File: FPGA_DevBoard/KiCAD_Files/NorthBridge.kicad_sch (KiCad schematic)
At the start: 15 parts, among them J1 4677, J2 DM3D-SF, U1 W25Q128JVSIQ TR, U14 ESP32-WROOM-32UE-N8

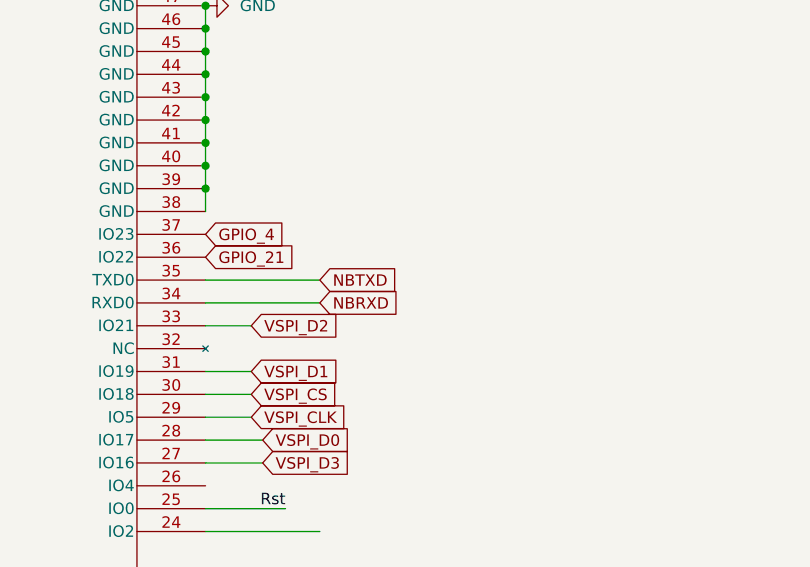
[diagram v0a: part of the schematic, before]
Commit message: ESD
Added ESD to the main USB programmer. Also added terminating resistors and test points. Also updated some planes to make sure everything was connected.
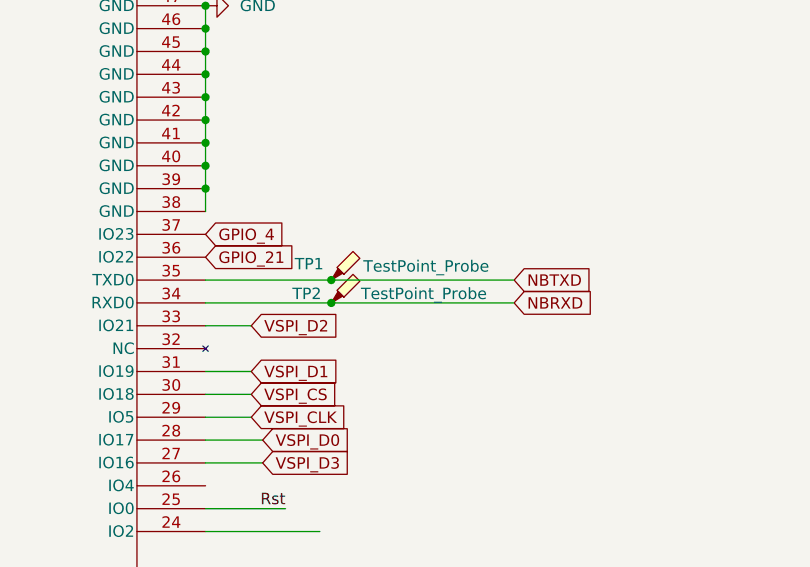
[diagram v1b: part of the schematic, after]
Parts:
- added TP1, TP2: TestPoint_Probe, TestPoint:TestPoint_Pad_D1.0mm, symbol Connector:TestPoint_Probe
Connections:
- net NBRXD: now also TP2.1
- net NBTXD: now also TP1.1
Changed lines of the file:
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@@
 	)
 	(junction
+		(at 113.03 95.25)
+		(diameter 0)
+		(color 0 0 0 0)
+	)
+	(junction
+		(at 113.03 92.71)
+		(diameter 0)
+		(color 0 0 0 0)
+	)
+	(junction
 		(at 99.06 64.77)
 		(diameter 0)
@@
 	(wire
 		(pts
-			(xy 99.06 92.71) (xy 111.76 92.71)
+			(xy 99.06 92.71) (xy 113.03 92.71)
 		)
 		(stroke
@@
 	(wire
 		(pts
+			(xy 113.03 95.25) (xy 133.35 95.25)
+		)
+		(stroke
+			(width 0)
+			(type default)
+		)
+	)
+	(wire
+		(pts
 			(xy 59.69 167.64) (xy 36.83 167.64)
 		)
@@
 	(wire
 		(pts
-			(xy 99.06 95.25) (xy 111.76 95.25)
+			(xy 99.06 95.25) (xy 113.03 95.25)
 		)
 		(stroke
@@
 	(wire
 		(pts
+			(xy 113.03 92.71) (xy 133.35 92.71)
+		)
+		(stroke
+			(width 0)
+			(type default)
+		)
+	)
+	(wire
+		(pts
 			(xy 255.27 134.62) (xy 257.81 134.62)
 		)
@@
 	(global_label "NBTXD"
 		(shape input)
-		(at 111.76 92.71 0)
+		(at 133.35 92.71 0)
 		(fields_autoplaced yes)
 		(effects
@@
 		)
 		(property "Intersheetrefs" "${INTERSHEET_REFS}"
-			(at 120.7928 92.71 0)
+			(at 142.3828 92.71 0)
 			(effects
 				(font
@@
 	(global_label "NBRXD"
 		(shape input)
-		(at 111.76 95.25 0)
+		(at 133.35 95.25 0)
 		(fields_autoplaced yes)
 		(effects
@@
 		)
 		(property "Intersheetrefs" "${INTERSHEET_REFS}"
-			(at 121.0952 95.25 0)
+			(at 142.6852 95.25 0)
 			(effects
 				(font
@@
 	)
 	(symbol
+		(lib_id "Connector:TestPoint_Probe")
+		(at 113.03 92.71 0)
+		(unit 1)
+		(exclude_from_sim no)
+		(in_bom yes)
+		(on_board yes)
+		(dnp no)
+		(property "Reference" "TP1"
+			(at 108.966 90.932 0)
+			(effects
+				(font
+					(size 1.27 1.27)
+				)
+				(justify left)
+			)
+		)
+		(property "Value" "TestPoint_Probe"
+			(at 116.586 91.186 0)
+			(effects
+				(font
+					(size 1.27 1.27)
+				)
+				(justify left)
+			)
+		)
+		(property "Footprint" "TestPoint:TestPoint_Pad_D1.0mm"
+			(at 118.11 92.71 0)
+			(effects
+				(font
+					(size 1.27 1.27)
+				)
+				(hide yes)
+			)
+		)
+		(property "Datasheet" "~"
+			(at 118.11 92.71 0)
+			(effects
+				(font
+					(size 1.27 1.27)
+				)
+				(hide yes)
+			)
+		)
+		(property "Description" "test point (alternative probe-style design)"
+			(at 113.03 92.71 0)
+			(effects
+				(font
+					(size 1.27 1.27)
+				)
+				(hide yes)
+			)
+		)
+		(pin "1"
+		)
+		(instances
+			(project ""
+				(path "/29dacc10-fb0d-42da-8b4b-fe903faf3f1a/3a4f201e-91d1-46c6-b180-b9c29ee81c31"
+					(reference "TP1")
+					(unit 1)
+				)
+			)
+		)
+	)
+	(symbol
 		(lib_id "Device:R_US")
 		(at 36.83 161.29 0)
@@
 					(unit 1)
 				)
+			)
+		)
+	)
+	(symbol
+		(lib_id "Connector:TestPoint_Probe")
+		(at 113.03 95.25 0)
+		(unit 1)
+		(exclude_from_sim no)
+		(in_bom yes)
+		(on_board yes)
+		(dnp no)
+		(property "Reference" "TP2"
+			(at 108.712 94.234 0)
+			(effects
+				(font
+					(size 1.27 1.27)
+				)
+				(justify left)
+			)
+		)
+		(property "Value" "TestPoint_Probe"
+			(at 116.332 94.234 0)
+			(effects
+				(font
+					(size 1.27 1.27)
+				)
+				(justify left)
+			)
+		)
+		(property "Footprint" "TestPoint:TestPoint_Pad_D1.0mm"
+			(at 118.11 95.25 0)
+			(effects
+				(font
+					(size 1.27 1.27)
+				)
+				(hide yes)
+			)
+		)
+		(property "Datasheet" "~"
+			(at 118.11 95.25 0)
+			(effects
+				(font
+					(size 1.27 1.27)
+				)
+				(hide yes)
+			)
+		)
+		(property "Description" "test point (alternative probe-style design)"
+			(at 113.03 95.25 0)
+			(effects
+				(font
+					(size 1.27 1.27)
+				)
+				(hide yes)
+			)
+		)
+		(pin "1"
+		)
+		(instances
+			(project "FPGA_DevBoard"
+				(path "/29dacc10-fb0d-42da-8b4b-fe903faf3f1a/3a4f201e-91d1-46c6-b180-b9c29ee81c31"
+					(reference "TP2")
+					(unit 1)
+				)

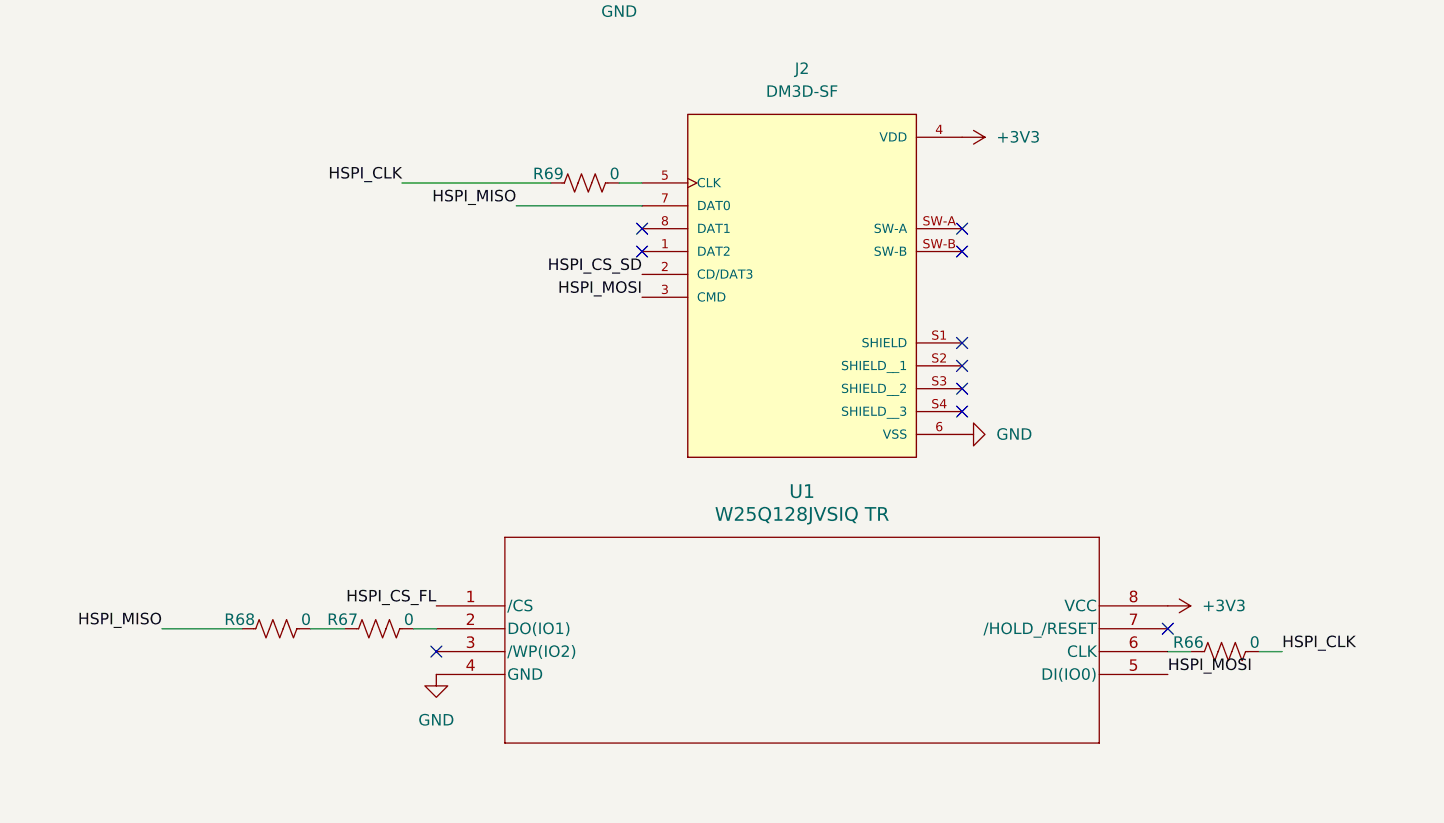
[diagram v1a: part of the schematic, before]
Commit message: FTDI
Added EEPROM To FTDI. Updated NB SPI bus. Added Debug LEDs to FTDI chip - PWREN and SUSPEND
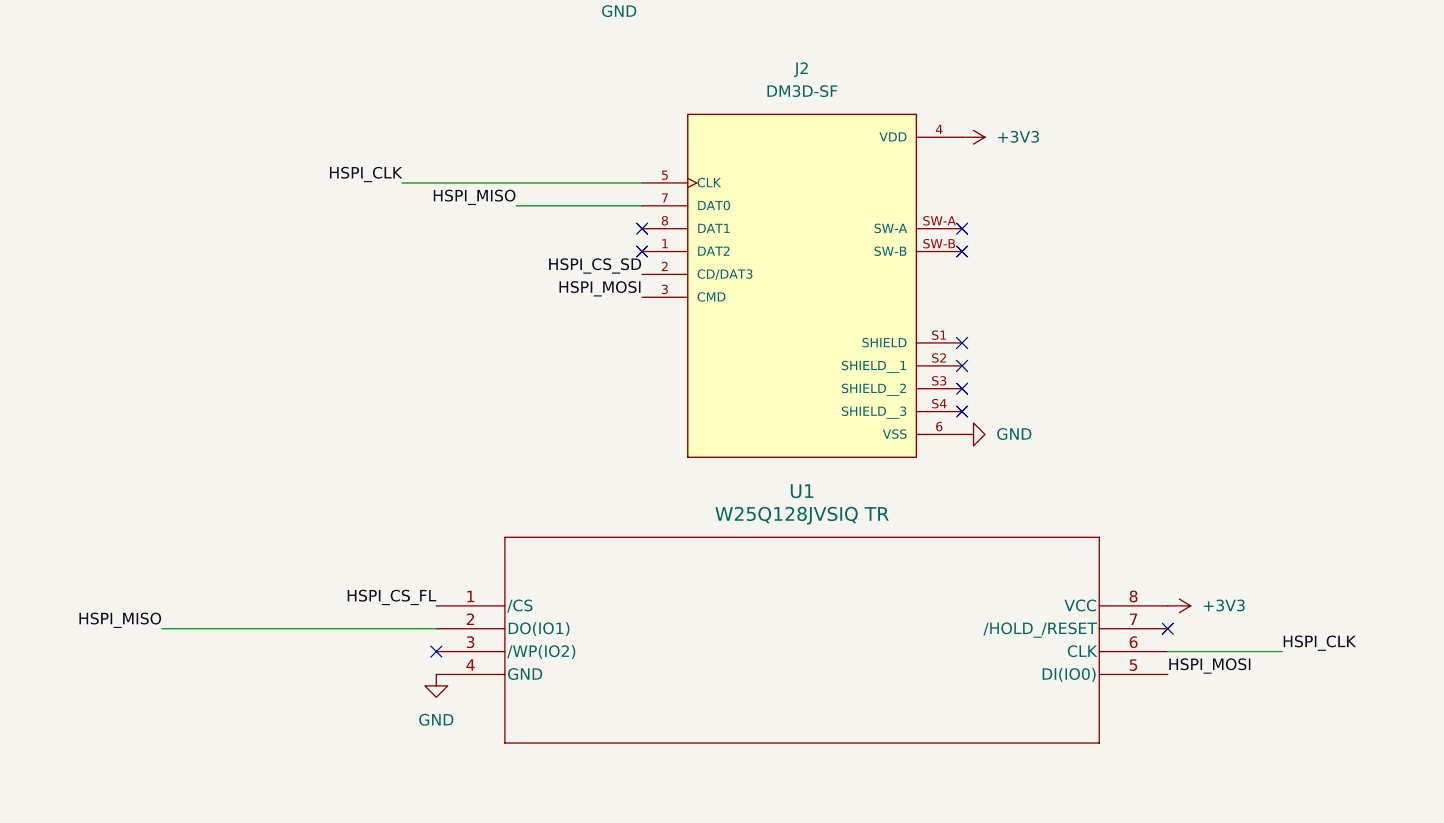
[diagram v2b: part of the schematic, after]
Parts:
- removed R66, R67, R68, R69: 0, Resistor_SMD:R_0402_1005Metric, symbol Device:R_US
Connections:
- net HSPI_CLK: now also J2.5 (CLK), U1.6 (CLK)
- net HSPI_MISO: now also U1.2 (DO(IO1))

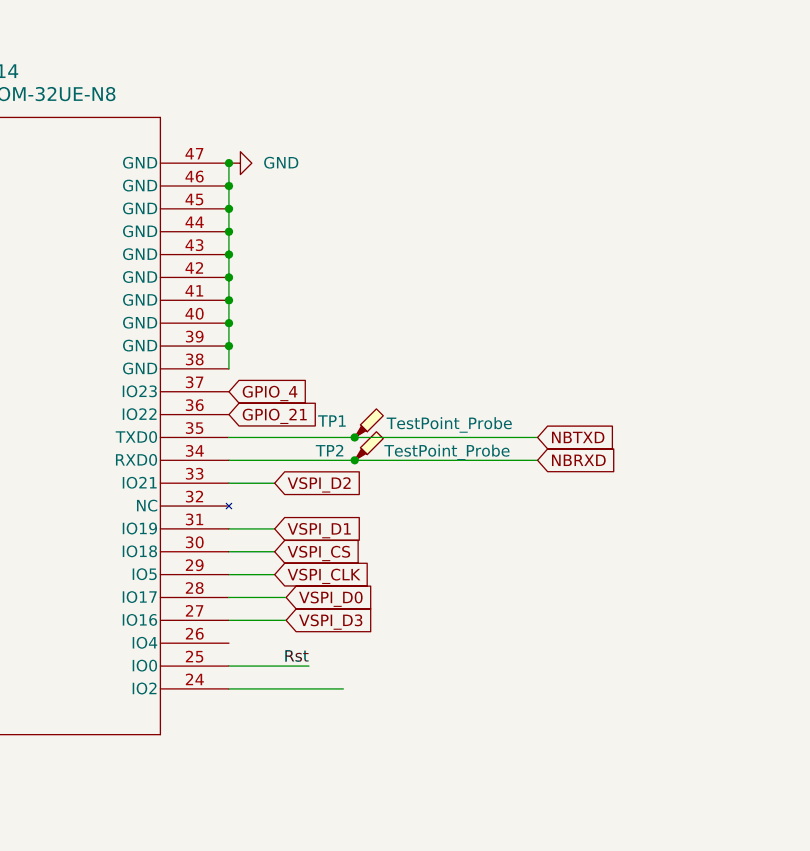
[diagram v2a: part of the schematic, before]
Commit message: Updated the NBSB IO to not go to input only, need to change this on the layout. Updated the FPGA clk to go to a positive differential signal with MCRR - need to change on layout. Updated the USB-UART bridge to not have Regin grounded - need to change on layout.
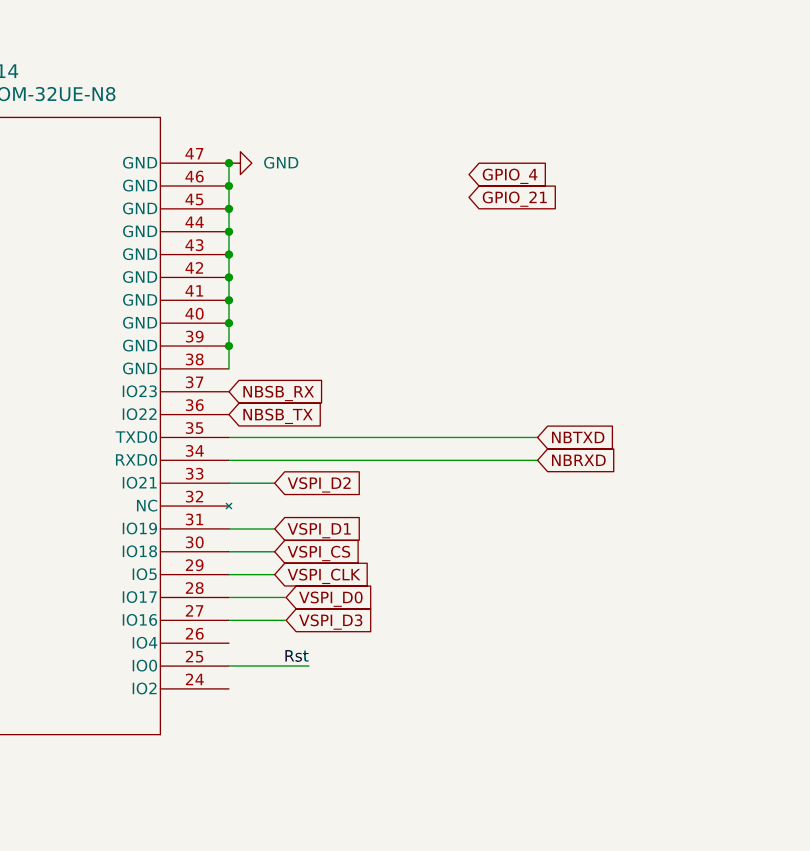
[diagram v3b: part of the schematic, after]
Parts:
- removed TP1, TP2: TestPoint_Probe, TestPoint:TestPoint_Pad_D1.0mm, symbol Connector:TestPoint_Probe
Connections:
- net GPIO_21: no longer U14.36 (IO22)
- net GPIO_4: no longer U14.37 (IO23)
- net NBSB_RX: now also U14.37 (IO23)
- net NBSB_TX: now also U14.36 (IO22)

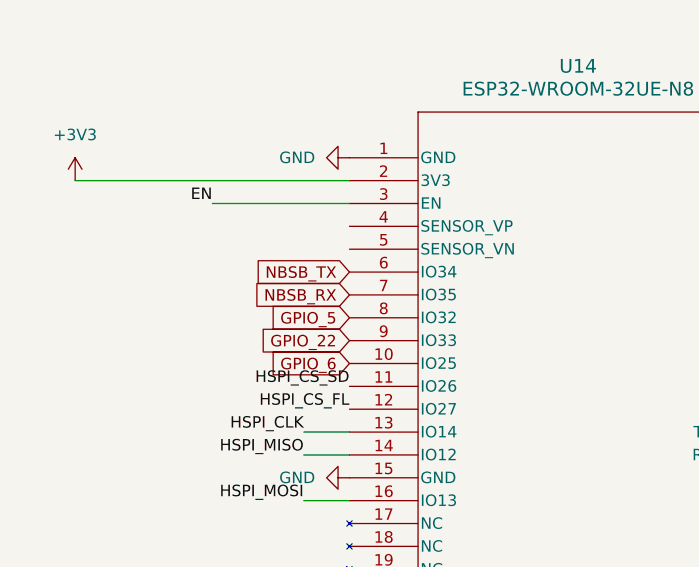
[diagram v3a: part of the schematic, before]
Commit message: Updated the layout to remove the JTAG header, connect the proper lines for the UART, and connect the proper pins for the audio.
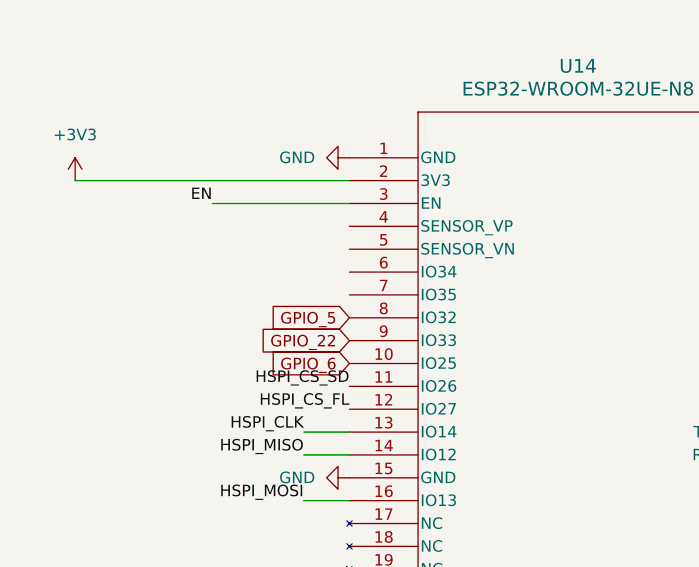
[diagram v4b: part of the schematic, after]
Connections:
- net NBSB_RX: no longer U14.7 (IO35)
- net NBSB_TX: no longer U14.6 (IO34)
